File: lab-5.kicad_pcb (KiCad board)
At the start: 4 copper layers, 39.9 x 68.9 mm, 63 parts, among them J1 Conn_01x04_Pin, J2 USB_C_Receptacle, J3 Conn_01x15_Pin, J4 Conn_01x15_Pin, SW1 NRST, SW2 BOOT, SW3 USER, U1 LM66100DCK, U2 LM66100DCK, U3 STM32F405RGTx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

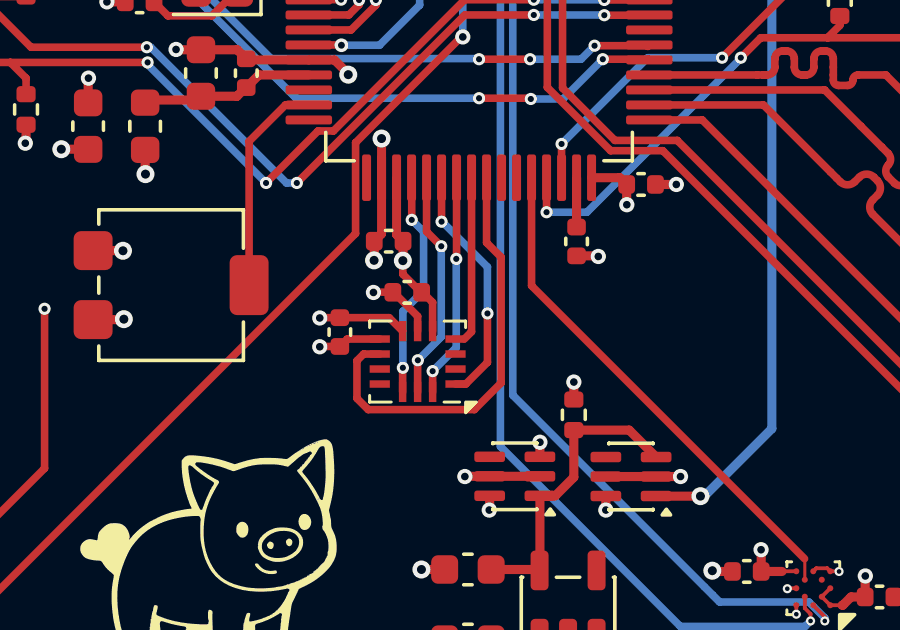
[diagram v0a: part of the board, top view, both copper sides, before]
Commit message: changed spi1 tracks lengh
Signed-off-by: Yehor Bilous <bilous801@gmail.com>
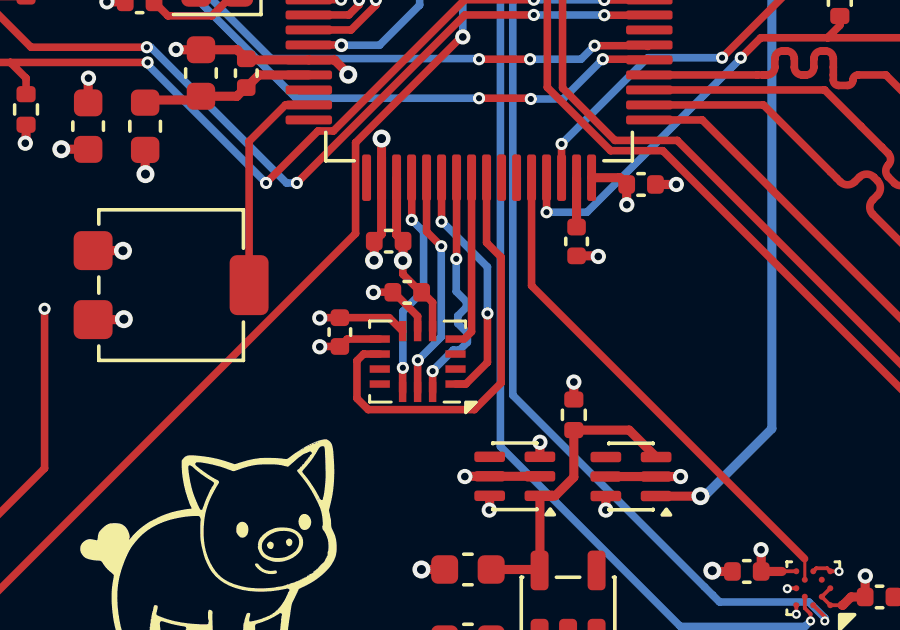
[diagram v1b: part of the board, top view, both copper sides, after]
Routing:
- net /SPI1_MOSI: track 7.47 -> 8.14 mm
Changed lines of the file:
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@@
 		(capping no)
 		(filling no)
-		(zone_defaults)
 		(pcbplotparams
 			(layerselection 0x00000000_00000000_55555555_5755f5ff)
@@
 	)
 	(segment
+		(start 156.99 107.22)
+		(end 156.99 106.13)
+		(width 0.254)
+		(layer "B.Cu")
+		(net "/SPI1_MOSI")
+	)
+	(segment
 		(start 156.2025 109.8725)
-		(end 156.99 109.085)
+		(end 156.2025 109.8575)
 		(width 0.254)
 		(layer "B.Cu")
@@
 	)
 	(segment
-		(start 156.99 109.085)
-		(end 156.99 106.13)
+		(start 157.04 108.03)
+		(end 157.33 107.74)
+		(width 0.254)
+		(layer "B.Cu")
+		(net "/SPI1_MOSI")
+	)
+	(segment
+		(start 156.2025 109.8575)
+		(end 156.89 109.17)
+		(width 0.254)
+		(layer "B.Cu")
+		(net "/SPI1_MOSI")
+	)
+	(segment
+		(start 157.33 107.56)
+		(end 156.99 107.22)
+		(width 0.254)
+		(layer "B.Cu")
+		(net "/SPI1_MOSI")
+	)
+	(segment
+		(start 157.04 108.28)
+		(end 157.04 108.03)
+		(width 0.254)
+		(layer "B.Cu")
+		(net "/SPI1_MOSI")
+	)
+	(segment
+		(start 157.33 107.74)
+		(end 157.33 107.56)
+		(width 0.254)
+		(layer "B.Cu")
+		(net "/SPI1_MOSI")
+	)
+	(segment
+		(start 157.36 108.6)
+		(end 157.04 108.28)
+		(width 0.254)
+		(layer "B.Cu")
+		(net "/SPI1_MOSI")
+	)
+	(segment
+		(start 156.89 109.17)
+		(end 157.1 109.17)
+		(width 0.254)
+		(layer "B.Cu")
+		(net "/SPI1_MOSI")
+	)
+	(segment
+		(start 157.36 108.91)
+		(end 157.36 108.6)
+		(width 0.254)
+		(layer "B.Cu")
+		(net "/SPI1_MOSI")
+	)
+	(segment
+		(start 157.1 109.17)
+		(end 157.36 108.91)
 		(width 0.254)
 		(layer "B.Cu")

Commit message: last
Signed-off-by: Yehor Bilous <bilous801@gmail.com>
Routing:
- net /SPI1_NSS: track 7.59 -> 8.21 mm
- net /SPI1_SCK: track 7.67 -> 8.18 mm
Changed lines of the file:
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@@
+	)
+	(segment
+		(start 155.72 106.49)
+		(end 155.72 106.409593)
+		(width 0.254)
+		(layer "B.Cu")
+		(net "/SPI1_NSS")
+	)
+	(segment
+		(start 155.12 107.09)
+		(end 155.72 106.49)
+		(width 0.254)
+		(layer "B.Cu")
+		(net "/SPI1_NSS")
+	)
+	(segment
+		(start 155.72 105.45)
+		(end 155.49 105.22)
+		(width 0.254)
+		(layer "B.Cu")
+		(net "/SPI1_NSS")
+	)
+	(segment
+		(start 155.72 106.409593)
+		(end 155.7259 106.403693)
+		(width 0.254)
+		(layer "B.Cu")
+		(net "/SPI1_NSS")
+	)
+	(segment
+		(start 155.21 109.75)
+		(end 154.83 109.37)
+		(width 0.254)
+		(layer "B.Cu")
+		(net "/SPI1_NSS")
+	)
+	(segment
+		(start 155.12 107.34)
+		(end 155.12 107.09)
+		(width 0.254)
+		(layer "B.Cu")
+		(net "/SPI1_NSS")
+	)
+	(segment
+		(start 154.81 107.65)
+		(end 155.12 107.34)
+		(width 0.254)
+		(layer "B.Cu")
+		(net "/SPI1_NSS")
 	)
 	(segment
 		(start 155.21 109.76)
-		(end 155.21 107.88)
-		(width 0.254)
-		(layer "B.Cu")
-		(net "/SPI1_NSS")
-	)
-	(segment
-		(start 155.9 105.2244)
+		(end 155.21 109.75)
+		(width 0.254)
+		(layer "B.Cu")
+		(net "/SPI1_NSS")
+	)
+	(segment
+		(start 154.81 107.88)
+		(end 154.81 107.65)
+		(width 0.254)
+		(layer "B.Cu")
+		(net "/SPI1_NSS")
+	)
+	(segment
+		(start 155.72 105.970407)
+		(end 155.72 105.45)
+		(width 0.254)
+		(layer "B.Cu")
+		(net "/SPI1_NSS")
+	)
+	(segment
+		(start 155.49 105.22)
+		(end 155.5056 105.2044)
+		(width 0.254)
+		(layer "B.Cu")
+		(net "/SPI1_NSS")
+	)
+	(segment
+		(start 155.21 109.76)
+		(end 155.21 109.69)
+		(width 0.2)
+		(layer "B.Cu")
+		(net "/SPI1_NSS")
+	)
+	(segment
+		(start 155.7259 106.403693)
+		(end 155.7259 105.976307)
+		(width 0.254)
+		(layer "B.Cu")
+		(net "/SPI1_NSS")
+	)
+	(segment
+		(start 155.5056 105.2044)
 		(end 155.5056 104.83)
 		(width 0.254)
@@
 	)
 	(segment
-		(start 155.21 107.88)
-		(end 155.9 107.19)
-		(width 0.254)
-		(layer "B.Cu")
-		(net "/SPI1_NSS")
-	)
-	(segment
-		(start 155.9 107.19)
-		(end 155.9 105.2244)
+		(start 154.83 109.37)
+		(end 154.83 109.12)
+		(width 0.254)
+		(layer "B.Cu")
+		(net "/SPI1_NSS")
+	)
+	(segment
+		(start 155.25 108.32)
+		(end 154.81 107.88)
+		(width 0.254)
+		(layer "B.Cu")
+		(net "/SPI1_NSS")
+	)
+	(segment
+		(start 155.7259 105.976307)
+		(end 155.72 105.970407)
+		(width 0.254)
+		(layer "B.Cu")
+		(net "/SPI1_NSS")
+	)
+	(segment
+		(start 154.83 109.12)
+		(end 155.25 108.7)
+		(width 0.254)
+		(layer "B.Cu")
+		(net "/SPI1_NSS")
+	)
+	(segment
+		(start 155.25 108.7)
+		(end 155.25 108.32)
 		(width 0.254)
 		(layer "B.Cu")
@@
 	)
 	(segment
-		(start 156.49 108.73)
+		(start 156 109.01)
+		(end 155.72 108.73)
+		(width 0.254)
+		(layer "B.Cu")
+		(net "/SPI1_SCK")
+	)
+	(segment
+		(start 156.41 107.54)
+		(end 156.41 107.413333)
+		(width 0.254)
+		(layer "B.Cu")
+		(net "/SPI1_SCK")
+	)
+	(segment
+		(start 155.71 109.51)
+		(end 156 109.22)
+		(width 0.254)
+		(layer "B.Cu")
+		(net "/SPI1_SCK")
+	)
+	(segment
+		(start 155.96 107.99)
+		(end 156.41 107.54)
+		(width 0.254)
+		(layer "B.Cu")
+		(net "/SPI1_SCK")
+	)
+	(segment
+		(start 156.28 107)
+		(end 156.58 106.7)
+		(width 0.254)
+		(layer "B.Cu")
+		(net "/SPI1_SCK")
+	)
+	(segment
+		(start 156.37 105.83)
 		(end 156.49 105.71)
-		(width 0.254)
-		(layer "B.Cu")
-		(net "/SPI1_SCK")
-	)
-	(segment
-		(start 155.71 109.51)
-		(end 156.49 108.73)
-		(width 0.254)
-		(layer "B.Cu")
+		(width 0.2)
+		(layer "B.Cu")
+		(net "/SPI1_SCK")
+	)
+	(segment
+		(start 156.28 107.18)
+		(end 156.28 107.12)
+		(width 0.2)
+		(layer "B.Cu")
+		(net "/SPI1_SCK")
+	)
+	(segment
+		(start 155.96 108.26)
+		(end 155.96 107.99)
+		(width 0.254)
+		(layer "B.Cu")
+		(net "/SPI1_SCK")
+	)
+	(segment
+		(start 156.58 106.7)
+		(end 156.58 106.51)
+		(width 0.254)
+		(layer "B.Cu")
+		(net "/SPI1_SCK")
+	)
+	(segment
+		(start 155.72 108.5)
+		(end 155.96 108.26)
+		(width 0.254)
+		(layer "B.Cu")
+		(net "/SPI1_SCK")
+	)
+	(segment
+		(start 156.41 107.31)
+		(end 156.28 107.18)
+		(width 0.254)
+		(layer "B.Cu")
+		(net "/SPI1_SCK")
+	)
+	(segment
+		(start 156.28 107.12)
+		(end 156.28 107)
+		(width 0.254)
+		(layer "B.Cu")
+		(net "/SPI1_SCK")
+	)
+	(segment
+		(start 156.58 106.51)
+		(end 156.37 106.3)
+		(width 0.254)
+		(layer "B.Cu")
+		(net "/SPI1_SCK")
+	)
+	(segment
+		(start 156.37 106.3)
+		(end 156.37 105.83)
+		(width 0.254)
+		(layer "B.Cu")
+		(net "/SPI1_SCK")
+	)
+	(segment
+		(start 156 109.22)
+		(end 156 109.01)
+		(width 0.254)
+		(layer "B.Cu")
+		(net "/SPI1_SCK")
+	)
+	(segment
+		(start 156.41 107.413333)
+		(end 156.41 107.31)
+		(width 0.254)
+		(layer "B.Cu")
+		(net "/SPI1_SCK")
+	)
+	(segment
+		(start 155.72 108.73)
+		(end 155.72 108.5)
+		(width 0.254)
+		(layer "B.Cu")
